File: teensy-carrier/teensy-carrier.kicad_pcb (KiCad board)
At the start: 2 copper layers, 56 x 18 mm, 3 parts, among them J1 Conn_01x02_Male, J2 Conn_01x15_Female, U1 Teensy3.2

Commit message: work on teensy-carrier
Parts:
- added J3: Conn_01x02_Female, Connector_PinHeader_2.54mm:PinHeader_1x02_P2.54mm_Horizontal, F.Cu at (709.0, 371.0)
- added REF**: MountingHole_3.2mm_M3, MountingHole:MountingHole_3.2mm_M3, F.Cu at (671.0, 379.5)
- added REF**: MountingHole_3.2mm_M3, MountingHole:MountingHole_3.2mm_M3, F.Cu at (719.0, 379.5)
- added REF**: bear, teensy:bear, B.Cu at (672.7, 366.5)
- added U2: LM1084-5.0, Package_TO_SOT_SMD:TO-263-3_TabPin2, F.Cu at (694.5, 372.3)
- J1: moved to F.Cu
- moved J1 15.3 mm to (680.5, 373.5)
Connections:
- J1 pad 2: +5V -> Net-(J1-Pad2)
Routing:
- net GND: vias 4 -> 7
- net +5V: vias 0 -> 25
- added copper zone on B.Cu, net +5V
- added copper zone on F.Cu, net Net-(J1-Pad2)
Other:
- board size 56 x 18 mm -> 56 x 34 mm
- board text added: "+5V"
- board text added: "GND"
- board text added: "Hirose FH19SC-15S"
- board text added: "LM1084/5/6-5.0 TO-263"
- board text added: "M3"
- board text added: "TEENSY 3.2 - Cut Vin/Vusb if LM108x installed"
- board text added: "UVTV Control & Power v1 SB Powell PhD samuel.powell@uq.edu.au"
- board text added: "VIN"
- board text added: "VIN MAX 25V"

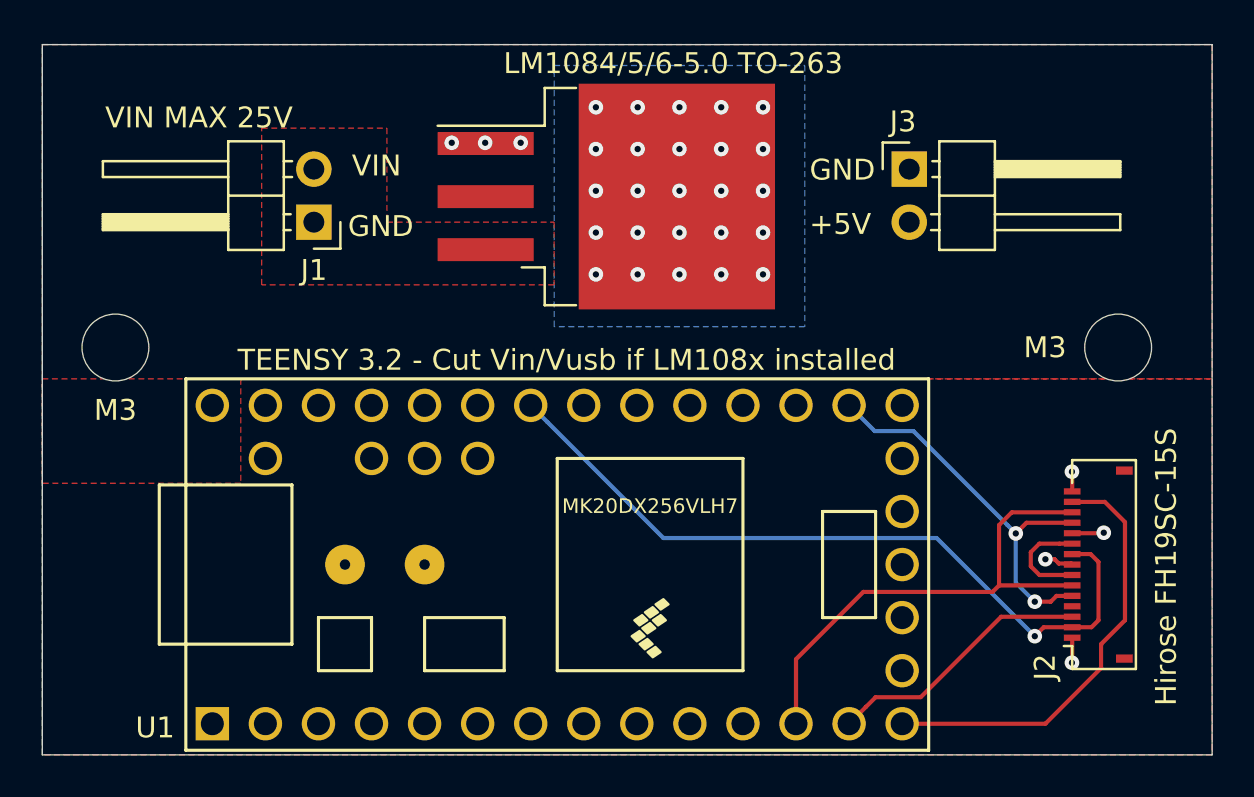
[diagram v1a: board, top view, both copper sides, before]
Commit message: fix reversed wiring
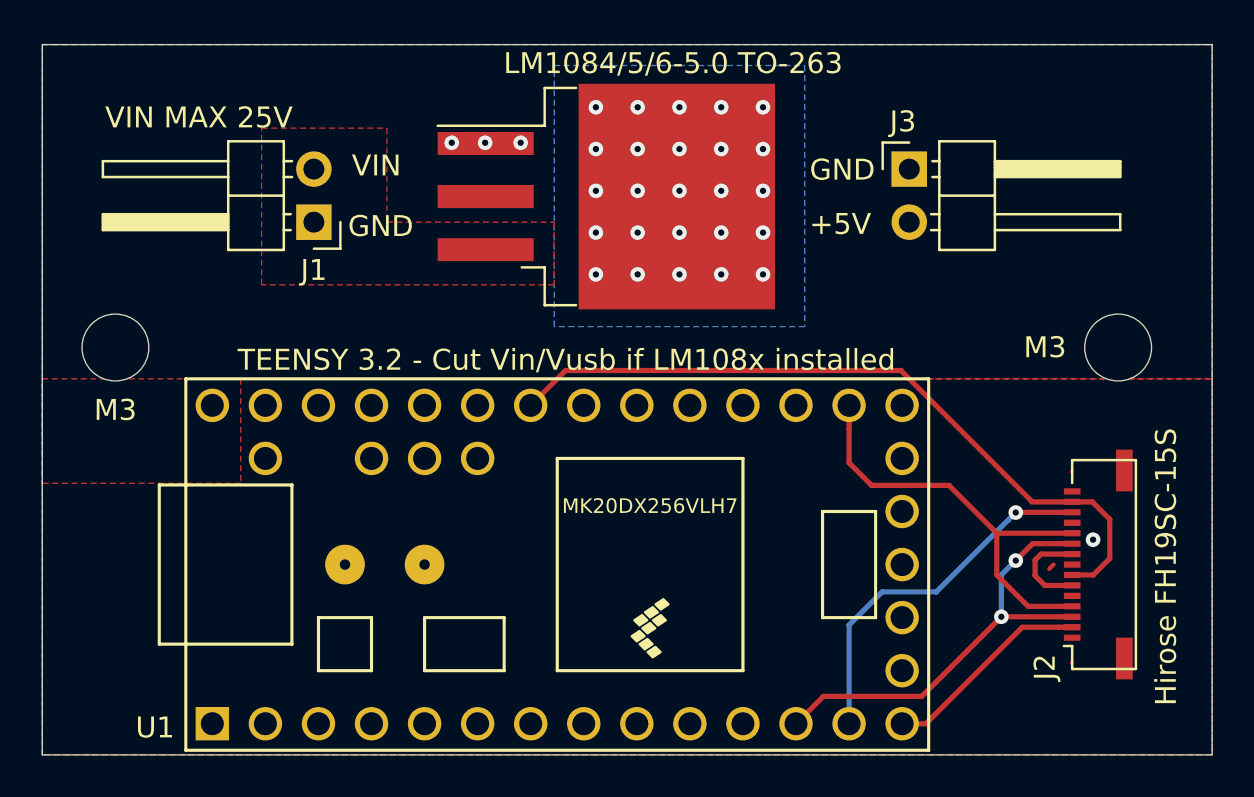
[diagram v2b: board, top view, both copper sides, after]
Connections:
- J2 pad 10: /SOUT1_SIN2 -> /LAT
- J2 pad 11: GND -> /SCLK
- J2 pad 12: /SCLK -> GND
- J2 pad 13: /LAT -> /SIN1
- J2 pad 14: /SOUT2 -> /GCLK
- J2 pad 2: /GCLK -> /SOUT2
- J2 pad 3: /SIN1 -> /LAT
- J2 pad 4: GND -> /SCLK
- J2 pad 5: /SCLK -> GND
- J2 pad 6: /LAT -> /SOUT1_SIN2
- J2 pad 7: /SOUT1_SIN2 -> /GCLK
- J2 pad 9: /GCLK -> /SOUT1_SIN2
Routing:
- net /SOUT2: track 21.0 -> 10.1 mm
- net /SIN1: track 12.8 -> 17.6 mm, vias 0 -> 1
- net GND: track 5.06 -> 0.33 mm, vias 7 -> 4
- net /LAT: track 24.4 -> 21.4 mm, vias 0 -> 2
- net /SCLK: track 19.0 -> 21.1 mm, vias 2 -> 0
- net /GCLK: track 36.3 -> 35.4 mm, vias 1 -> 0

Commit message: fix pin ordering, use terminal blocks instead of pin headers for power entry/supply
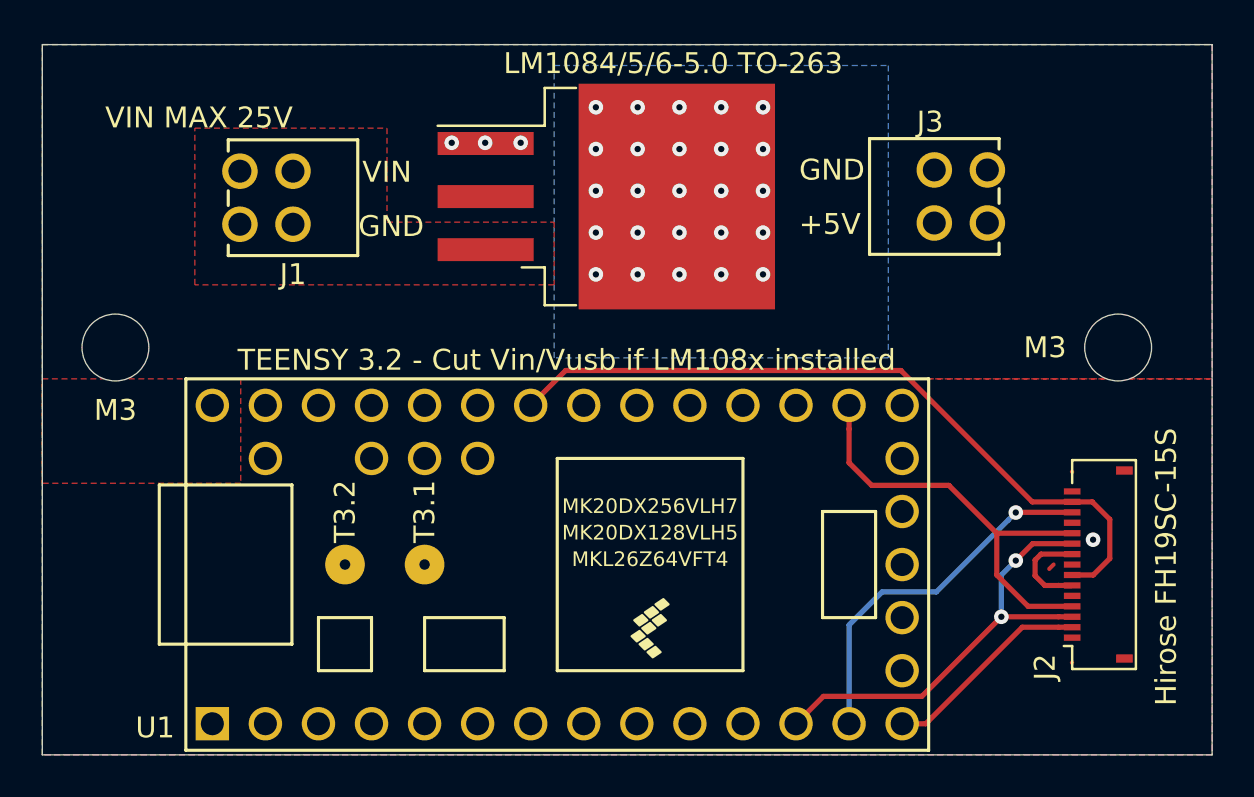
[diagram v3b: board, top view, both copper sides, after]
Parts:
- added REF**: nemo, teensy:nemo, B.Cu at (719.3, 368.9)
- J1, J3: footprint Connector_PinHeader_2.54mm:PinHeader_1x02_P2.54mm_Horizontal -> teensy:TerminalBlock_DECA-MB312-254-2
- moved J3 1.20 mm to (710.2, 371.0), turned to 270 degrees
- moved J1 1.00 mm to (679.5, 373.6), turned to 90 degrees
- moved REF** 0.22 mm to (672.5, 366.4)
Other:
- board text added: "UVTV Control & Power v2 SB Powell PhD samuel.powell@uq.edu.au"
- board text removed: "UVTV Control & Power v1 SB Powell PhD samuel.powell@uq.edu.au"
